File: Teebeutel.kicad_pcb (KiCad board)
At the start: 2 copper layers, 72 x 100 mm, 148 parts, among them J1 RJ45_Shielded, J2 Battery, J3 Micro_SD_Card, J4 Conn_01x30_Female, Q1 S8050, Q2 S8050, SW1 K1-1506SN-01, SW2 SW_SPST, U1 LIS2DE12, U10 SDB628, U11 TLV1117-33, U12 SGP30, U2 ESP32-WROOM-32, U3 SRV05-4, U4 TXB0104RUT, U5 MCP73831-2-OT, U6 PPSI262, U7 RM-V8xxC_TR1, U8 TLV70018_SOT23-5, U9 TXB0104RUT

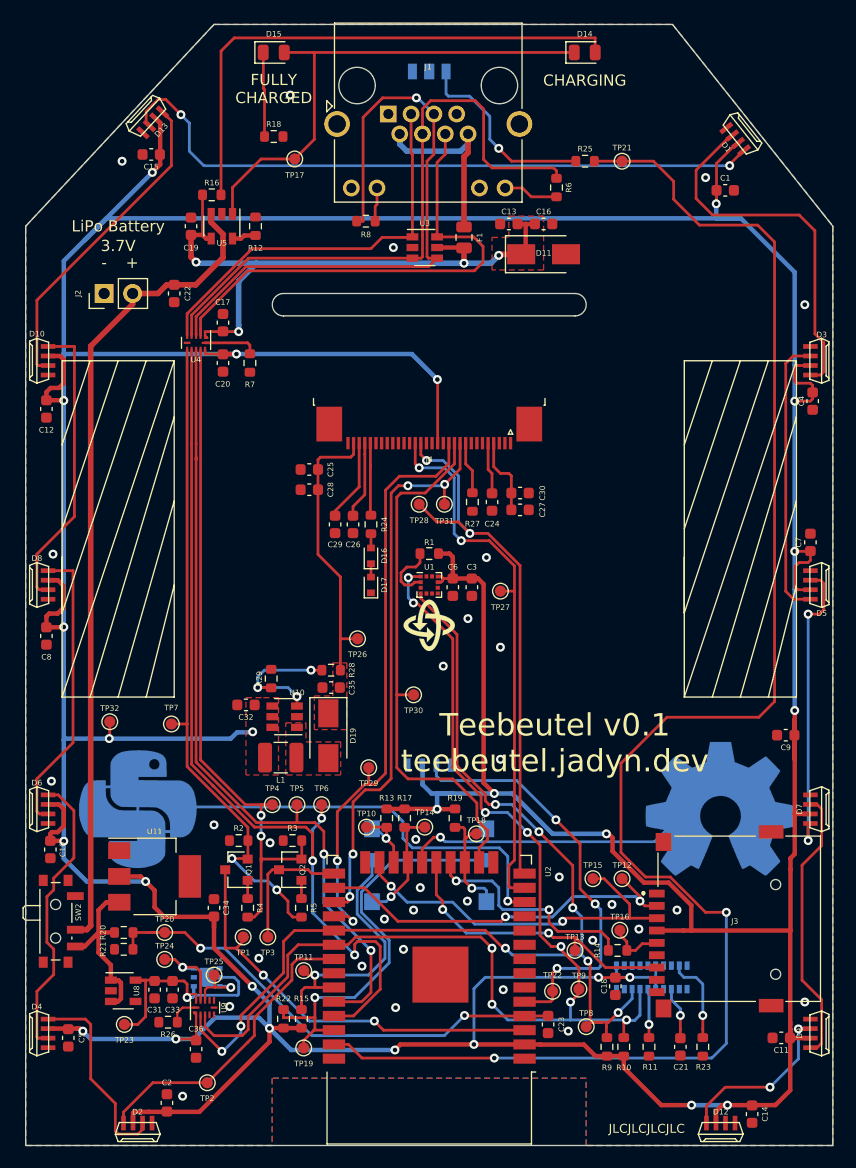
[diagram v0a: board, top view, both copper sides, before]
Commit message: feat(): Add 100nF and 10µF to ESP32-VCC
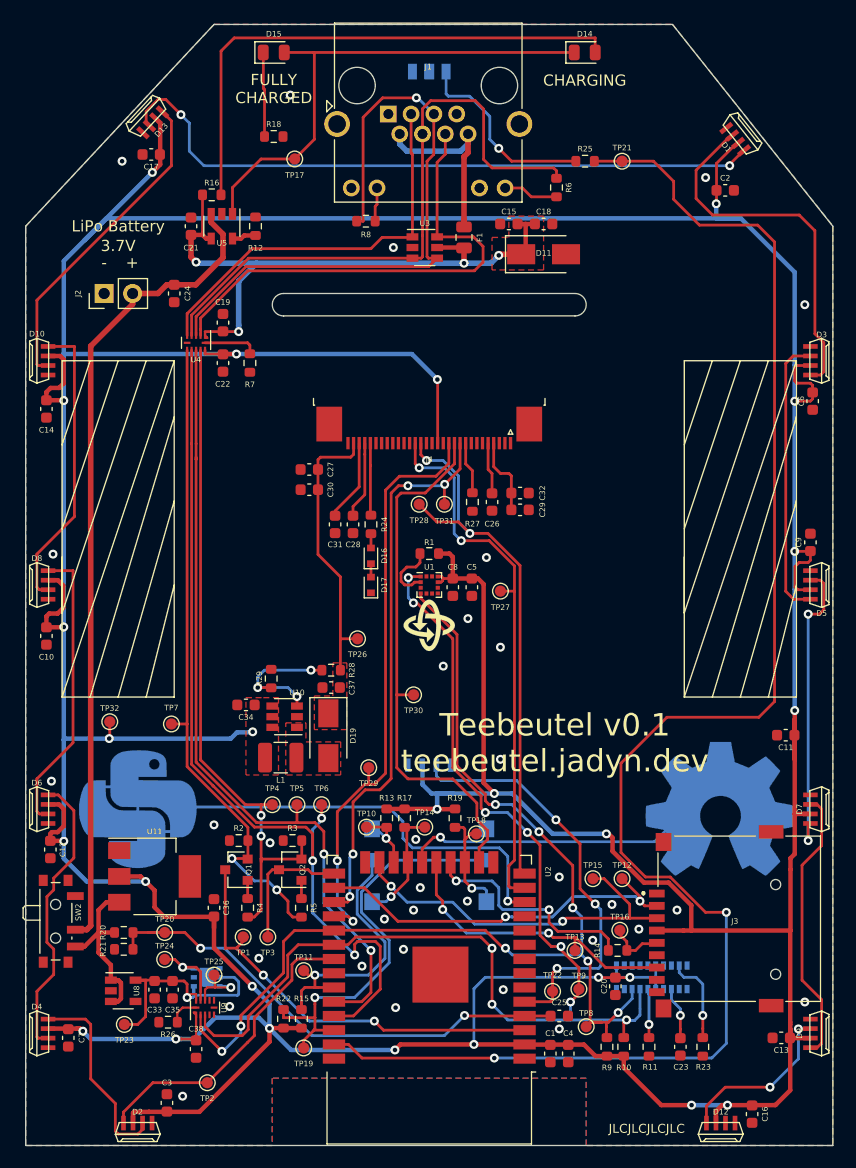
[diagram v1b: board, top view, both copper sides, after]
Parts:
- removed the C23 at (156.6, 139.2)
- added C1: 100n, Capacitor_SMD:C_0603_1608Metric, F.Cu at (156.8, 141.8)
- added C25: 100n, Capacitor_SMD:C_0603_1608Metric, F.Cu at (157.6, 138.4)
- added C4: 100n, Capacitor_SMD:C_0603_1608Metric, F.Cu at (158.4, 141.8)
- renumbered C8 to C10, C9 to C11, C10 to C12, C11 to C13, C12 to C14, C13 to C15, C14 to C16, C15 to C17, C16 to C18, C17 to C19, C1 to C2, C18 to C20, C19 to C21, C20 to C22, C21 to C23, C22 to C24, C24 to C26, C25 to C27, C26 to C28, C27 to C29, C2 to C3, C28 to C30, C29 to C31, C30 to C32, C31 to C33, C32 to C34, C33 to C35, C34 to C36, C35 to C37, C36 to C38, C3 to C5, C4 to C6, C5 to C7, C6 to C8, C7 to C9

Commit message: chore: Cleanup some files
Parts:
- C4: value 100n -> 10µ
- moved TP8 0.45 mm to (160.2, 139.0)
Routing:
- net I2C-SDA: track 98.2 -> 97.7 mm
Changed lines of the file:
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@@
     (thickness 1.6)
     (drawings 83)
-    (tracks 1184)
+    (tracks 1183)
     (zones 0)
     (modules 150)
@@
     (add_net "Net-(D10-Pad3)")
     (add_net "Net-(D12-Pad1)")
+    (add_net "Net-(D12-Pad3)")
     (add_net "Net-(D14-Pad1)")
     (add_net "Net-(D14-Pad2)")
@@
     (add_net "Net-(J1-Pad5)")
     (add_net "Net-(J1-Pad6)")
+    (add_net "Net-(J3-Pad1)")
     (add_net "Net-(J3-Pad5)")
+    (add_net "Net-(J3-Pad8)")
+    (add_net "Net-(J4-Pad19)")
+    (add_net "Net-(J4-Pad2)")
+    (add_net "Net-(J4-Pad25)")
     (add_net "Net-(J4-Pad26)")
+    (add_net "Net-(J4-Pad6)")
+    (add_net "Net-(J4-Pad7)")
+    (add_net "Net-(J4-Pad8)")
     (add_net "Net-(J4-Pad9)")
     (add_net "Net-(Q1-Pad1)")
@@
     (add_net "Net-(R28-Pad1)")
     (add_net "Net-(R7-Pad1)")
+    (add_net "Net-(SW2-Pad1)")
     (add_net "Net-(TP24-Pad1)")
     (add_net "Net-(TP25-Pad1)")
+    (add_net "Net-(U1-Pad11)")
+    (add_net "Net-(U1-Pad12)")
+    (add_net "Net-(U1-Pad3)")
+    (add_net "Net-(U10-Pad6)")
+    (add_net "Net-(U12-Pad4)")
+    (add_net "Net-(U2-Pad10)")
+    (add_net "Net-(U2-Pad11)")
+    (add_net "Net-(U2-Pad24)")
+    (add_net "Net-(U2-Pad32)")
+    (add_net "Net-(U2-Pad6)")
+    (add_net "Net-(U2-Pad7)")
+    (add_net "Net-(U2-Pad8)")
+    (add_net "Net-(U2-Pad9)")
+    (add_net "Net-(U6-Pad1)")
+    (add_net "Net-(U6-Pad10)")
+    (add_net "Net-(U6-Pad12)")
+    (add_net "Net-(U6-Pad13)")
+    (add_net "Net-(U6-Pad14)")
+    (add_net "Net-(U6-Pad17)")
+    (add_net "Net-(U6-Pad2)")
+    (add_net "Net-(U6-Pad20)")
+    (add_net "Net-(U6-Pad4)")
+    (add_net "Net-(U6-Pad9)")
+    (add_net "Net-(U8-Pad4)")
+    (add_net "Net-(U9-Pad4)")
+    (add_net "Net-(U9-Pad5)")
+    (add_net "Net-(U9-Pad7)")
+    (add_net "Net-(U9-Pad8)")
     (add_net OLED-CS)
     (add_net OLED-DC)
@@
       (effects (font (size 0.5 0.5) (thickness 0.1)))
     )
-    (fp_text value 100n (at 0 1.43 90) (layer F.Fab)
+    (fp_text value 10µ (at 0 1.43 90) (layer F.Fab)
       (effects (font (size 1 1) (thickness 0.15)))
     )
@@
   )
   (module TestPoint:TestPoint_Pad_D1.0mm (layer F.Cu)
-    (at 160 139.4)
+    (at 160.2 139)
     (descr "SMD pad as test Point, diameter 1.0mm")
     (tags "test point SMD pad")
@@
   (segment (start 160.14799 133.54799) (end 160.15 133.54799) (width 0.25) (layer B.Cu) (net 20))
   (segment (start 160.4 139) (end 161.8 139) (width 0.25) (layer F.Cu) (net 20))
-  (segment (start 160 139.4) (end 160.4 139) (width 0.25) (layer F.Cu) (net 20))
   (segment (start 151.334408 119.578226) (end 151.900093 119.578226) (width 0.25) (layer F.Cu) (net 20))
   (segment (start 148.477011 104.414511) (end 148.477011 116.143837) (width 0.25) (layer F.Cu) (net 20))

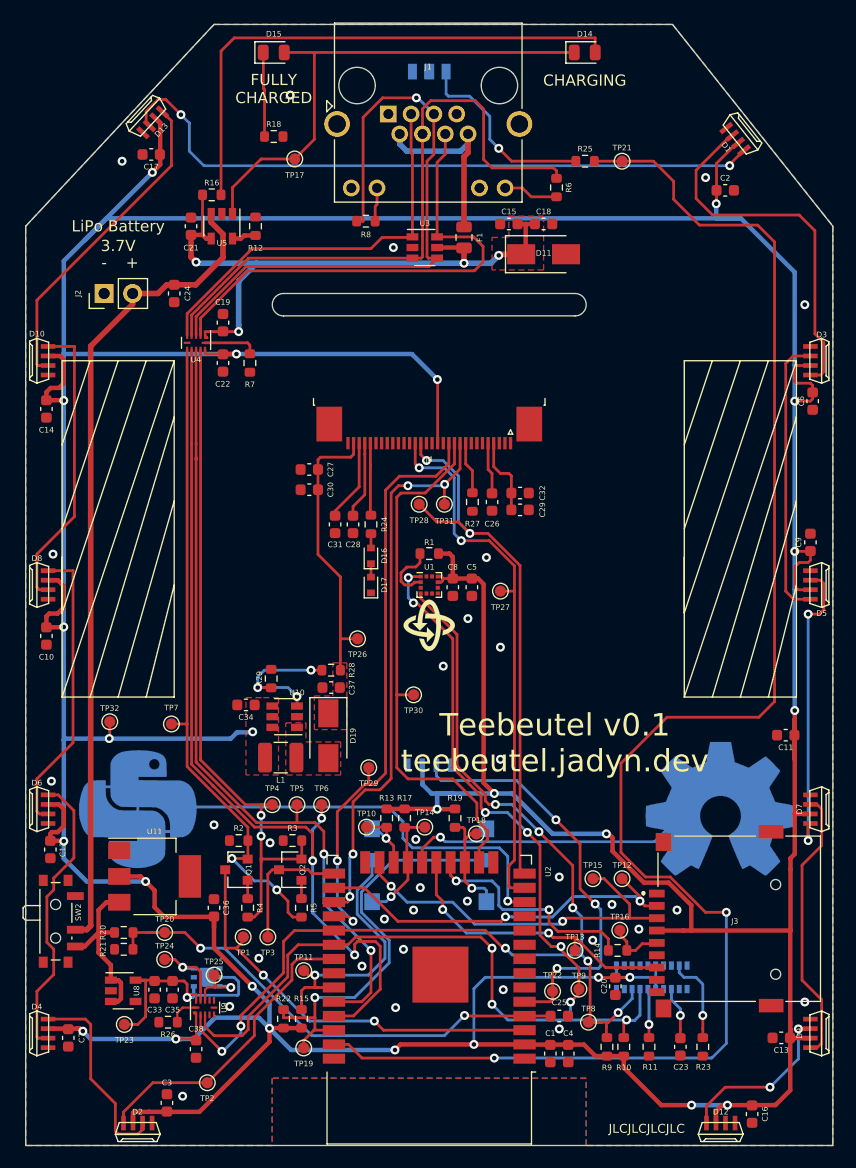
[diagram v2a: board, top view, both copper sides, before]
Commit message: feat(): add Cs to SD-Card Vcc
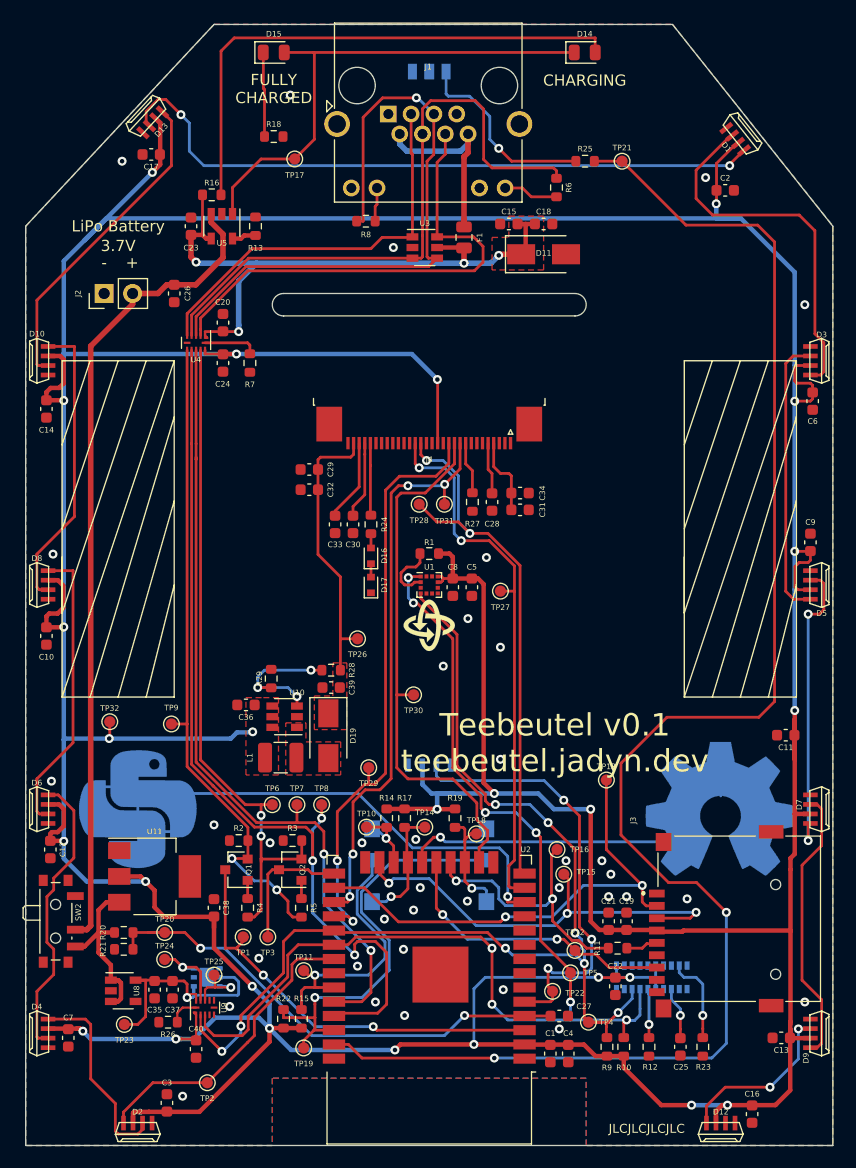
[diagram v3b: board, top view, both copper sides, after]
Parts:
- added C19: 100n, Capacitor_SMD:C_0603_1608Metric, F.Cu at (163.6, 130.0)
- added C21: 10µ, Capacitor_SMD:C_0603_1608Metric, F.Cu at (162.0, 130.0)
- moved TP16 9.12 mm to (157.4, 123.6)
- moved TP13 8.91 mm to (161.8, 117.4)
- moved TP15 2.63 mm to (158.0, 125.8)
- moved TP5 1.63 mm to (158.6, 134.6)
- moved R11 0.20 mm to (162.8, 132.4)
- renumbered C19 to C20, C20 to C22, C21 to C23, C22 to C24, C23 to C25, C24 to C26, C25 to C27, C26 to C28, C27 to C29, C28 to C30, C29 to C31, C30 to C32, C31 to C33, C32 to C34, C33 to C35, C34 to C36, C35 to C37, C36 to C38, C37 to C39, C38 to C40, R14 to R11, R11 to R12, R12 to R13, R13 to R14, TP13 to TP12, TP12 to TP13, TP8 to TP4, TP9 to TP5, TP4 to TP6, TP5 to TP7, TP6 to TP8, TP7 to TP9
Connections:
- TP16 pad 1: Net-(J3-Pad5) -> SD-SCK
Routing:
- net SD-CS: track 34.0 -> 43.8 mm
- net SD-MOSI: track 33.3 -> 39.4 mm, vias 2 -> 3
- net SD-SCK: track 20.2 -> 24.8 mm
- net I2C-SDA: track 97.7 -> 99.9 mm
- net Net-(J3-Pad5): track 5.01 -> 2.87 mm
- net IR-TX: track 144.8 -> 143.0 mm
- net RxD: track 80.5 -> 82.1 mm
- net IR-RX: track 37.7 -> 39.3 mm
- net TOUCH4: track 30.9 -> 32.0 mm
- net I2C-SCL: track 105.6 -> 106.5 mm, vias 9 -> 8
- net +3V3: track 567.1 -> 568.0 mm
- net TOUCH9: track 39.3 -> 38.5 mm
- net GND: vias 32 -> 36

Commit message: chore: update refs, bom, documentation
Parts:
- renumbered TP16 to TP10, TP13 to TP11, TP15 to TP12, TP12 to TP13, TP10 to TP14, TP11 to TP15, TP14 to TP16, TP18 to TP17, TP19 to TP18, TP17 to TP19

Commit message: feat(): Add name-tag, stencil tooling holes, OSHW-Information
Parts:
- added G***: LOGO, Teebeutel_Graphics:name-tag, F.Cu at (129.0, 94.8)
- added REF**: OSHW-Logo2_7.3x6mm_SilkScreen, Symbol:OSHW-Logo2_7.3x6mm_SilkScreen, F.Cu at (168.6, 71.8)
- moved TP30 5.40 mm to (144.6, 115.2)
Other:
- board text added: "ID: *TBA*"
